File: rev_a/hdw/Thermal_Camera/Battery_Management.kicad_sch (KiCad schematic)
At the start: 0 parts

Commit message: added battery circuitry, LCD backlight
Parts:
- added C? (x2): 10uF, Capacitors_SMD:C_0603, symbol Custom_Library:C_Custom
- added C? (x6): 10uF, Capacitors_SMD:C_1206, symbol Custom_Library:C_Custom
- added C? (x3): 1uF, Capacitors_SMD:C_0603, symbol Custom_Library:C_Custom
- added C?: 0.1uF, Capacitors_SMD:C_0603, symbol Custom_Library:C_Custom
- added C?: C, Capacitors_SMD:C_0603, symbol Custom_Library:C_Custom
- added DOC?: 0x55, symbol Custom Library:I2C_Address
- added L?: L, Inductors_SMD:L_Vishay_IHLP-2020, symbol Custom_Library:L_Custom
- added R? (x3): R, Resistors_SMD:R_0603, symbol Custom_Library:R_Custom
- added R? (x4): 100k, Resistors_SMD:R_0603, symbol Custom_Library:R_Custom
- added R? (x2): 10k, Resistors_SMD:R_0603, symbol Custom_Library:R_Custom
- added R? (x2): 0.02, Resistors_SMD:R_0612, symbol Custom_Library:R_Custom
- added R? (x3): 10K, Resistors_SMD:R_0603, symbol Custom_Library:R_Custom
- added U?: BQ27441DRZT-G1A, Package_SON:Texas_S-PDSO-N12, symbol Battery_Management:BQ27441DRZT-G1A
- added U?: MAX8903, Package_DFN_QFN:QFN-28-1EP_4x4mm_P0.4mm_EP2.6x2.6mm, symbol Custom Library:MAX8903
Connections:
- new net: R?.1, U?.11 (IDC)
- new net: C?.1, R?.1, U?.5 (V_{DD})
- new net: C?.1, R?.1, U?.9 (VL)
- new net: C?.1, U?.10 (CT)
- new net: R?.1, U?.13 (ISET)
- new net: L?.1, U?.25 (CS), U?.26 (CS)
- new net: C?.2, L?.2, U?.27 (LX), U?.28 (LX)
- new net: C?.1, U?.6 (BST)
- new net +12V: C?.1, C?.1, U?.3 (DC), U?.4 (DC), U?.5 (DCM)
- new net +3.0V: R?.1, R?.1, R?.1, R?.1, R?.1
- new net BATT_IUSB: R?.1, U?.7 (IUSB)
- new net BATT_LOWBAT: R?.2, U?.12 (GPOUT)
- new net BATT_NTC: R?.2, R?.2, U?.10 (BIN), U?.16 (THM)
- new net BATT_SNS-: C?.1, C?.1, R?.1, R?.1, U?.20 (BAT), U?.21 (BAT), U?.7 (SRN)
- new net GND: C?.2, C?.2, C?.2, C?.2, C?.2, C?.2, C?.2, C?.2, C?.2, C?.2, C?.2, C?.2, R?.2, R?.2, R?.2, R?.2, R?.2, U?.1 (PG), U?.12 (GND), U?.13 (PAD), U?.2 (PG), U?.29 (EP), U?.3 (V_{SS})
- new net I2C_SCL: U?.2 (SCL)
- new net I2C_SDA: U?.1 (SDA)
- new net USB_SUSPEND: R?.1, U?.15 (USUS)
- new net VBAT: C?.1, R?.2, R?.2, U?.6 (BAT), U?.8 (SRP)
- new net VBUS: C?.1, C?.1, U?.17 (USB)
- new net VCOM: C?.1, C?.1, U?.23 (SYS), U?.24 (SYS)
- new net ~{BATT_CEN}: R?.1, U?.14 (~{CEN})
- new net ~{BATT_CHG}: R?.2, U?.22 (~{CHG})
- new net ~{BATT_DOK}: R?.2, U?.8 (~{DOK})
- new net ~{BATT_FLT}: R?.2, U?.18 (~{FLT})
- new net ~{BATT_UOK}: R?.2, U?.19 (~{UOK})
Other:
- note added: "For +4.2V Battery"
- note added: "This fuel gauge is sketchy Want to find battery with NTC"

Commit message: added PIC32 bypass, SD card load switch, other random junk
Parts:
- R?: value R -> 1.8M
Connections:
- net VBUS renamed +5V_USB
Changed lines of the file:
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@@
-    )
-  )
-  (symbol (lib_id "power:VBUS") (at 69.85 92.71 0) (unit 1)
-    (in_bom yes) (on_board yes) (dnp no)
-    (property "Reference" "#PWR06" (at 69.85 96.52 0)
-      (effects (font (size 1.27 1.27)) hide)
-    )
-    (property "Value" "VBUS" (at 69.85 88.9 0)
-      (effects (font (size 1.27 1.27)))
-    )
-    (property "Footprint" "" (at 69.85 92.71 0)
-      (effects (font (size 1.27 1.27)) hide)
-    )
-    (property "Datasheet" "" (at 69.85 92.71 0)
-      (effects (font (size 1.27 1.27)) hide)
-    )
-    (pin "1")
-    (instances
-      (project "Thermal_Camera"
-        (path "/4bd21e0b-5408-4b93-866e-c82ac5b31fa9/079d68a7-d67d-4f5f-9c02-dfffe75c3c82"
-          (reference "#PWR06") (unit 1)
-        )
-      )
     )
   )
@@
       (effects (font (size 1.27 1.27)) (justify right))
     )
-    (property "Value" "R" (at 43.18 171.45 90)
+    (property "Value" "1.8M" (at 43.18 171.45 90)
       (effects (font (size 1.27 1.27)))
     )
@@
     )
   )
+  (symbol (lib_id "Custom Library:+5V_USB") (at 69.85 92.71 0) (unit 1)
+    (in_bom yes) (on_board yes) (dnp no)
+    (property "Reference" "#PWR06" (at 69.85 96.52 0)
+      (effects (font (size 1.27 1.27)) hide)
+    )
+    (property "Value" "+5V_USB" (at 69.85 89.154 0)
+      (effects (font (size 1.27 1.27)))
+    )
+    (property "Footprint" "" (at 69.85 92.71 0)
+      (effects (font (size 1.27 1.27)) hide)
+    )
+    (property "Datasheet" "" (at 69.85 92.71 0)
+      (effects (font (size 1.27 1.27)) hide)
+    )
+    (pin "1")
+    (instances
+      (project "Thermal_Camera"
+        (path "/4bd21e0b-5408-4b93-866e-c82ac5b31fa9/079d68a7-d67d-4f5f-9c02-dfffe75c3c82"
+          (reference "#PWR06") (unit 1)
+        )
+      )
+    )
+  )
   (symbol (lib_id "power:GND") (at 24.13 179.07 0) (unit 1)
     (in_bom yes) (on_board yes) (dnp no)
@@
     (in_bom yes) (on_board yes) (dnp no)
     (property "Reference" "R?" (at 180.34 62.23 90)
-      (effects (font (size 1.27 1.27)) hide)
+      (effects (font (size 1.27 1.27)))
     )
     (property "Value" "0.02" (at 180.34 59.69 90)

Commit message: added some more USB stuff
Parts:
- removed R?: 10K, Resistors_SMD:R_0603, symbol Custom_Library:R_Custom
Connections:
- net USB_SUSPEND renamed HUB_SUSPND

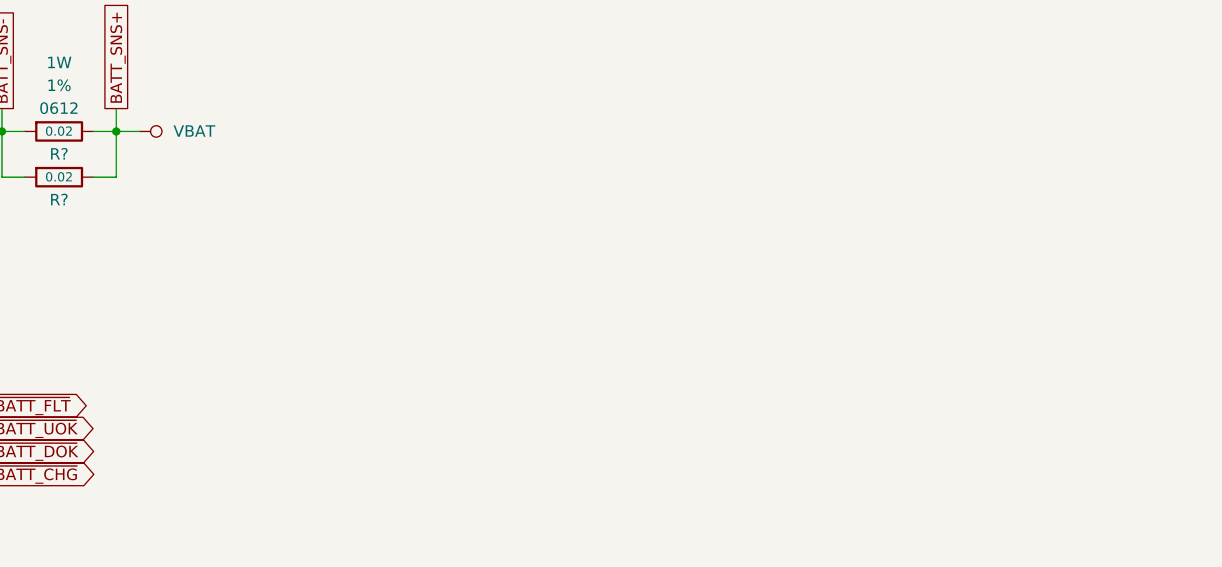
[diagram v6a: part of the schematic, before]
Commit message: added notes for battery
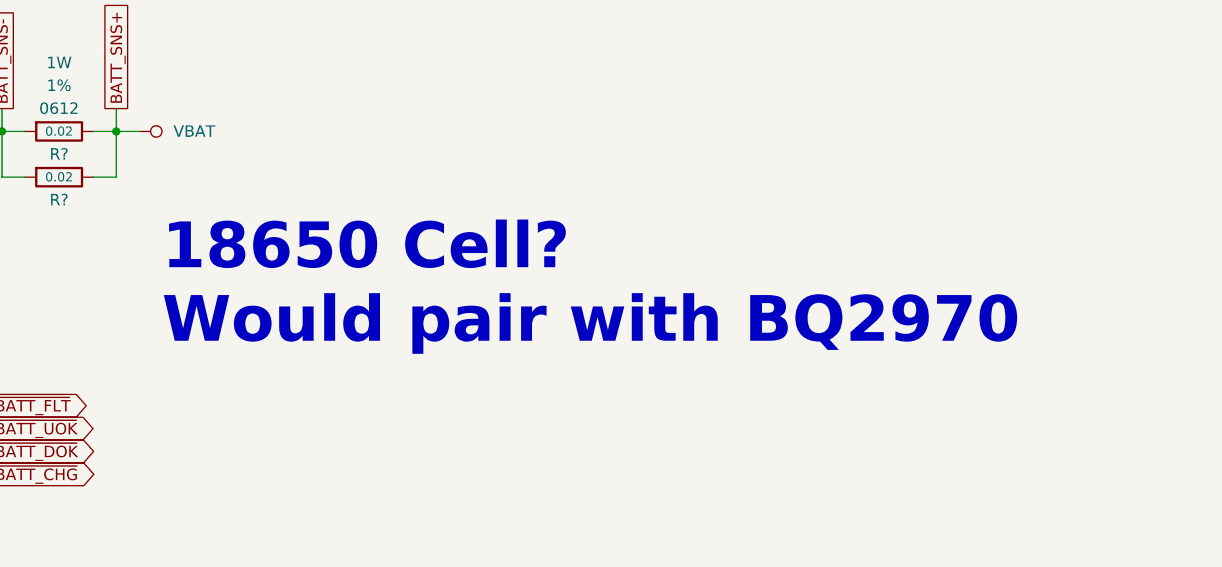
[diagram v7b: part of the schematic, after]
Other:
- note added: "18650 Cell? Would pair with BQ2970"
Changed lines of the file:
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@@
     (effects (font (face "Courier New") (size 2.54 2.54) (thickness 0.254) bold) (justify left bottom))
+  )
+  (text "18650 Cell?\nWould pair with BQ2970" (at 191.77 78.74 0)
+    (effects (font (size 5.08 5.08) (thickness 1.016) bold (color 194 0 0 1)) (justify left bottom))
   )
   (text "This fuel gauge is sketchy\nWant to find battery with NTC"

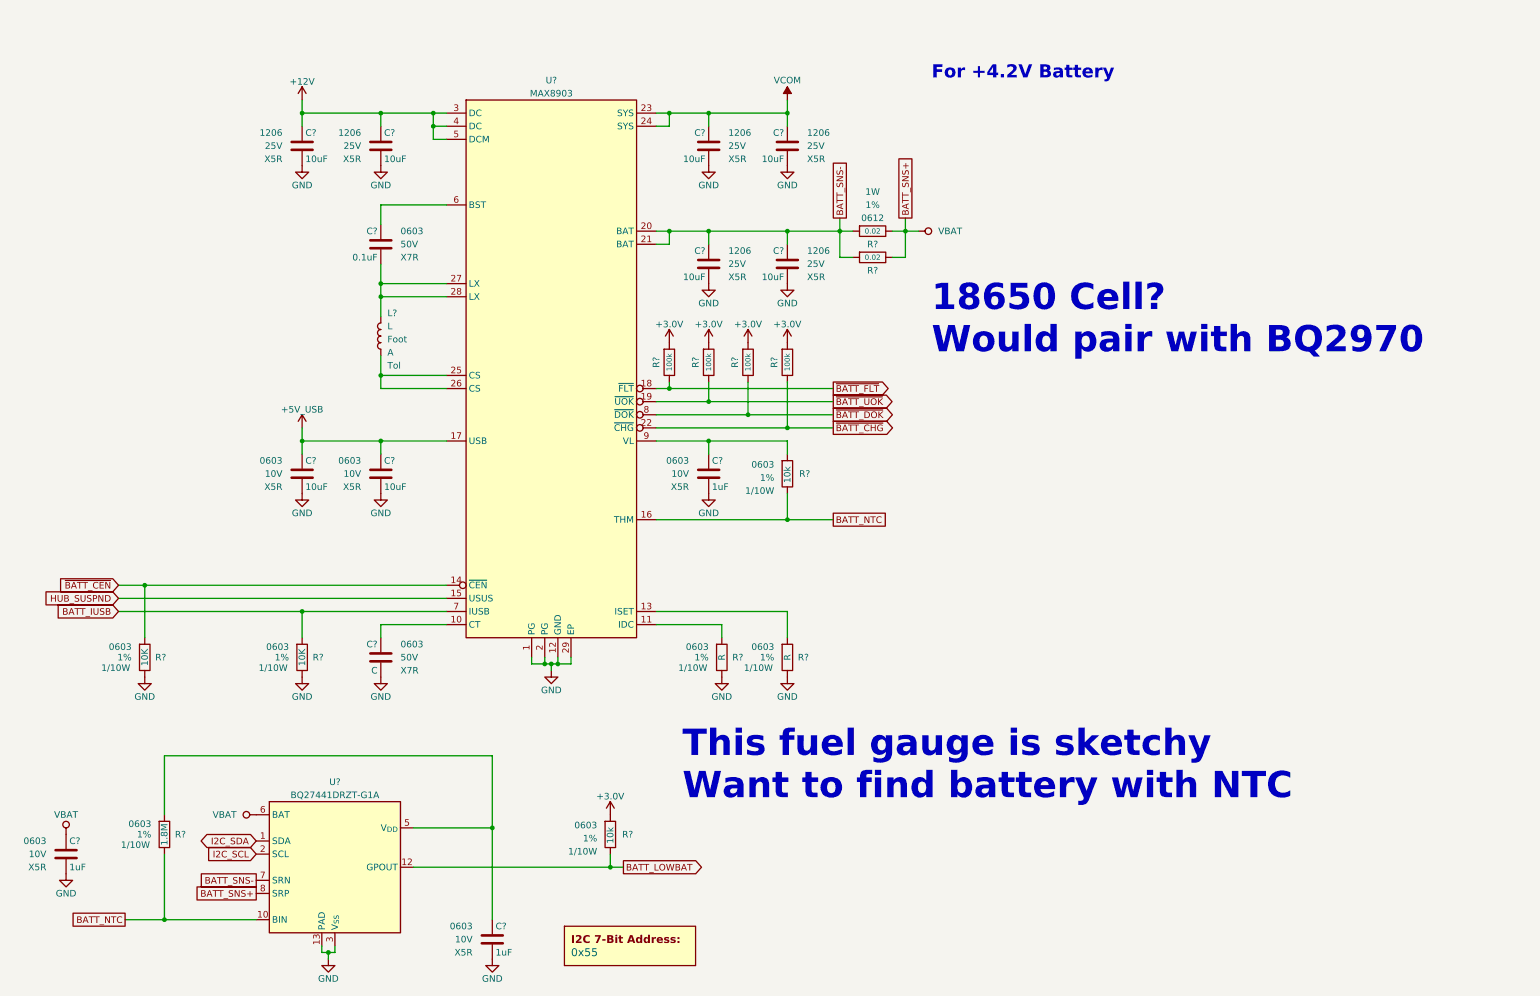
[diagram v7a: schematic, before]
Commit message: Added battery cell and protection IC
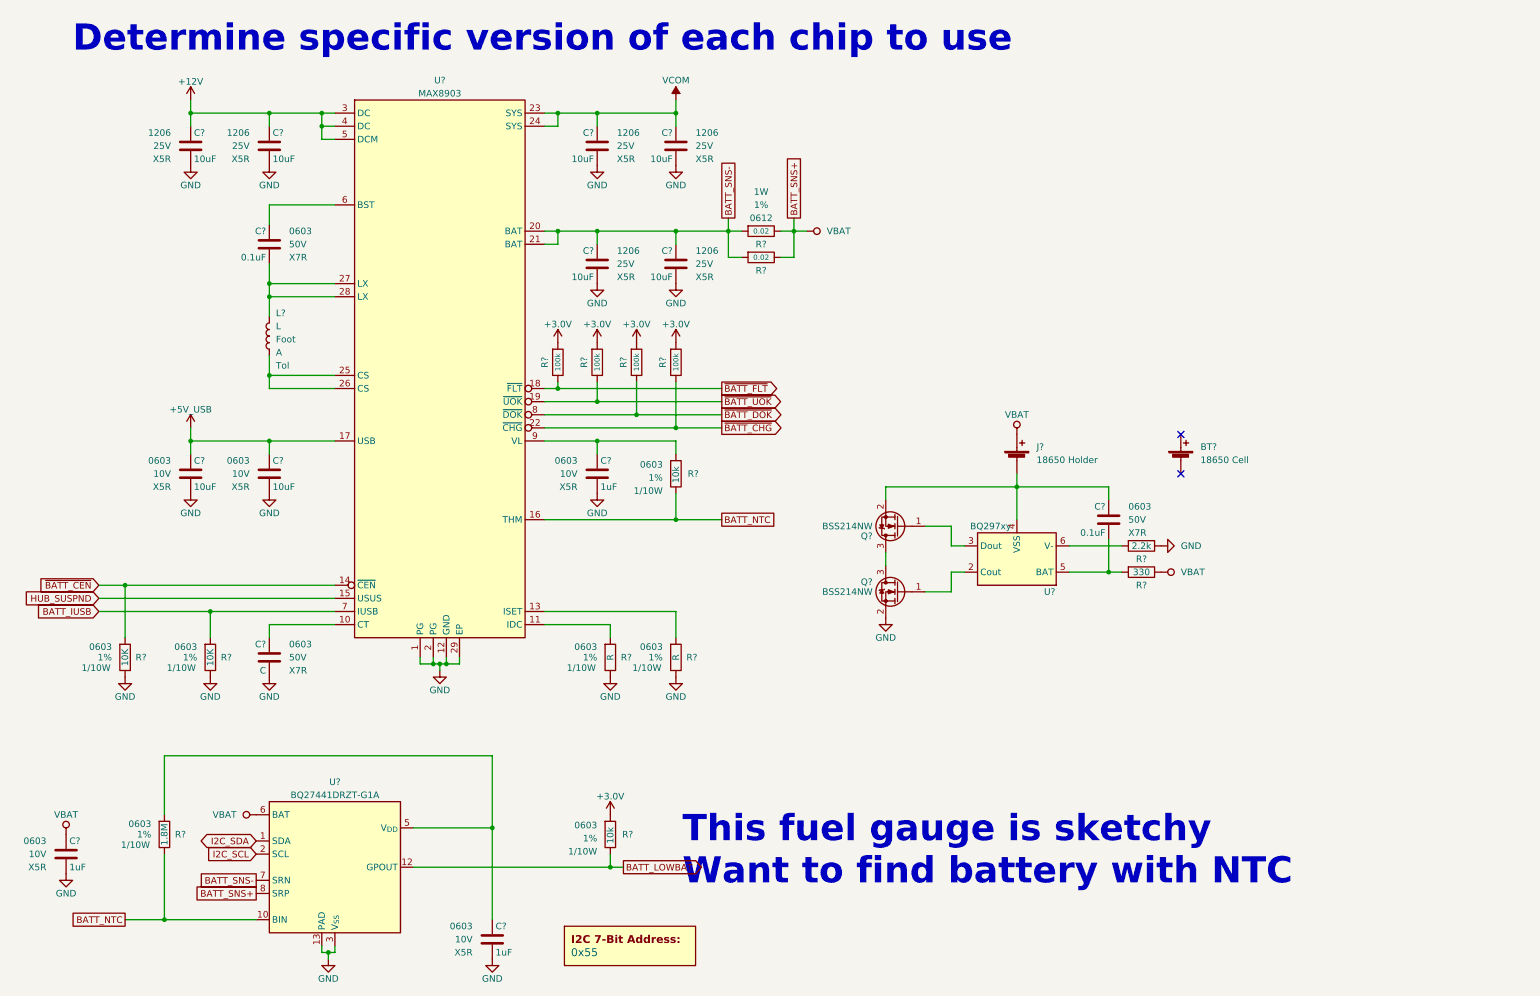
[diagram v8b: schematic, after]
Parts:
- added BT?: 18650 Cell, symbol Device:Battery_Cell
- added C?: 0.1uF, Capacitors_SMD:C_0603, symbol Custom_Library:C_Custom
- added J?: 18650 Holder, symbol Device:Battery_Cell
- added Q? (x2): BSS214NW, Package_TO_SOT_SMD:SOT-323_SC-70, symbol Transistor_FET:BSS214NW
- added R?: 2.2k, Resistors_SMD:R_0603, symbol Custom_Library:R_Custom
- added R?: 330, Resistors_SMD:R_0603, symbol Custom_Library:R_Custom
- added U?: BQ297xy, Package_SON:WSON-6_1.5x1.5mm_P0.5mm, symbol Battery_Management:BQ297xy
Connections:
- net GND: now also Q?.2 (S), R?.2
- net VBAT: now also J?.1 (+), R?.2
- new net: C?.1, J?.2 (-), Q?.2 (S), U?.4 (VSS)
- new net: C?.2, R?.1, U?.5 (BAT)
- new net: R?.1, U?.6 (V-)
- new net: Q?.1 (G), U?.2 (Cout)
- new net: Q?.1 (G), U?.3 (Dout)
- new net: Q?.3 (D), Q?.3 (D)
- no-connect marks 0 -> 2
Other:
- note added: "Determine specific version of each chip to use"
- note removed: "18650 Cell? Would pair with BQ2970"
- note removed: "For +4.2V Battery"
- moved on the sheet: C?, L?, R?, U?
